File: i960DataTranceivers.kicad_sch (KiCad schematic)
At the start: 6 parts

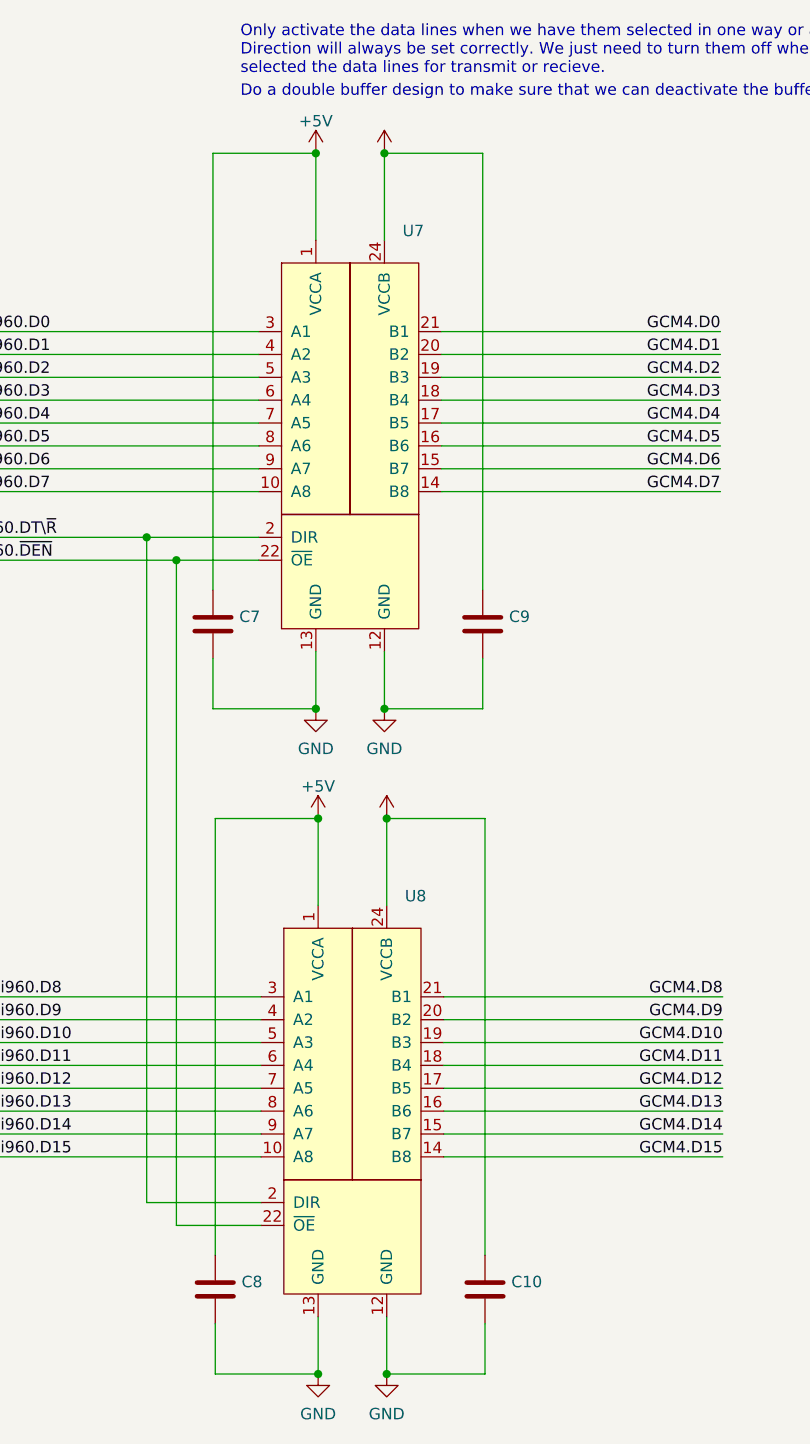
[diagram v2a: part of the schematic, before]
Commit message: Fix naming + more features
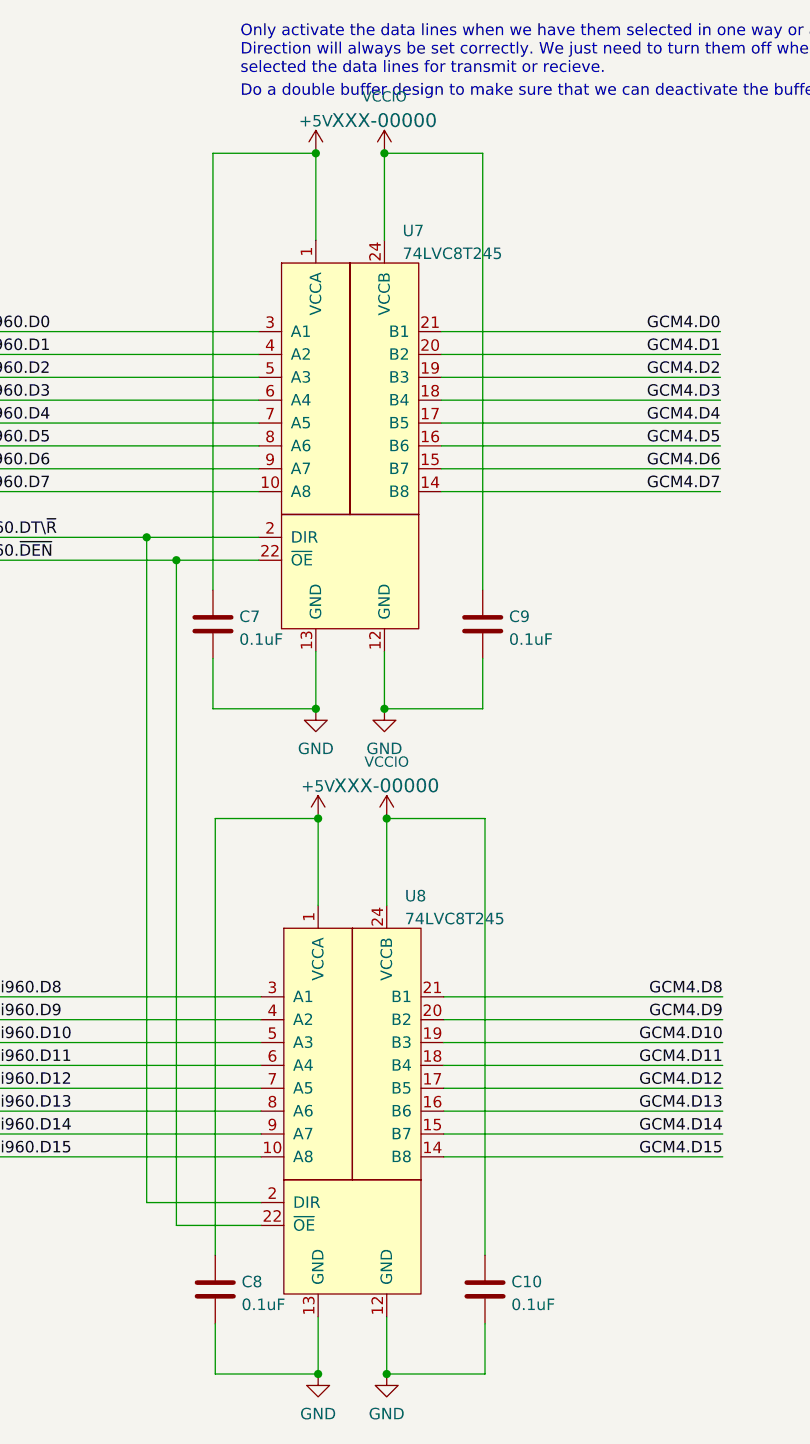
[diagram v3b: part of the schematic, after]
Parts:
- C10, C7, C8, C9: value (none) -> 0.1uF; footprint (none) -> Capacitor_SMD:C_0805_2012Metric_Pad1.18x1.45mm_HandSolder
- U7, U8: value (none) -> 74LVC8T245; footprint (none) -> Package_SO:SOIC-24W_7.5x15.4mm_P1.27mm
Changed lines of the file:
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@@
       (effects (font (size 1.27 1.27)) (justify left))
     )
-    (property "Value" "" (id 1) (at 132.5754 36.3021 0)
-      (effects (font (size 1.27 1.27)) (justify left))
-    )
-    (property "Footprint" "" (id 2) (at 126.746 66.548 0)
+    (property "Value" "74LVC8T245" (id 1) (at 132.5754 36.3021 0)
+      (effects (font (size 1.27 1.27)) (justify left))
+    )
+    (property "Footprint" "Package_SO:SOIC-24W_7.5x15.4mm_P1.27mm" (id 2) (at 126.746 66.548 0)
       (effects (font (size 1.27 1.27)) hide)
     )
@@
       (effects (font (size 1.27 1.27)) (justify left))
     )
-    (property "Value" "" (id 1) (at 144.653 153.0862 0)
-      (effects (font (size 1.27 1.27)) (justify left))
-    )
-    (property "Footprint" "" (id 2) (at 142.6972 155.194 0)
+    (property "Value" "0.1uF" (id 1) (at 144.653 153.0862 0)
+      (effects (font (size 1.27 1.27)) (justify left))
+    )
+    (property "Footprint" "Capacitor_SMD:C_0805_2012Metric_Pad1.18x1.45mm_HandSolder" (id 2) (at 142.6972 155.194 0)
       (effects (font (size 1.27 1.27)) hide)
     )
@@
       (effects (font (size 1.27 1.27)) (justify left))
     )
-    (property "Value" "" (id 1) (at 114.681 153.0862 0)
-      (effects (font (size 1.27 1.27)) (justify left))
-    )
-    (property "Footprint" "" (id 2) (at 112.7252 155.194 0)
+    (property "Value" "0.1uF" (id 1) (at 114.681 153.0862 0)
+      (effects (font (size 1.27 1.27)) (justify left))
+    )
+    (property "Footprint" "Capacitor_SMD:C_0805_2012Metric_Pad1.18x1.45mm_HandSolder" (id 2) (at 112.7252 155.194 0)
       (effects (font (size 1.27 1.27)) hide)
     )
@@
       (effects (font (size 1.27 1.27)) (justify left))
     )
-    (property "Value" "" (id 1) (at 144.399 79.1722 0)
-      (effects (font (size 1.27 1.27)) (justify left))
-    )
-    (property "Footprint" "" (id 2) (at 142.4432 81.28 0)
+    (property "Value" "0.1uF" (id 1) (at 144.399 79.1722 0)
+      (effects (font (size 1.27 1.27)) (justify left))
+    )
+    (property "Footprint" "Capacitor_SMD:C_0805_2012Metric_Pad1.18x1.45mm_HandSolder" (id 2) (at 142.4432 81.28 0)
       (effects (font (size 1.27 1.27)) hide)
     )
@@
       (effects (font (size 1.27 1.27)) (justify left))
     )
-    (property "Value" "" (id 1) (at 132.8294 110.2161 0)
-      (effects (font (size 1.27 1.27)) (justify left))
-    )
-    (property "Footprint" "" (id 2) (at 127 140.462 0)
+    (property "Value" "74LVC8T245" (id 1) (at 132.8294 110.2161 0)
+      (effects (font (size 1.27 1.27)) (justify left))
+    )
+    (property "Footprint" "Package_SO:SOIC-24W_7.5x15.4mm_P1.27mm" (id 2) (at 127 140.462 0)
       (effects (font (size 1.27 1.27)) hide)
     )
@@
       (effects (font (size 1.27 1.27)) (justify left))
     )
-    (property "Value" "" (id 1) (at 114.427 79.1722 0)
-      (effects (font (size 1.27 1.27)) (justify left))
-    )
-    (property "Footprint" "" (id 2) (at 112.4712 81.28 0)
+    (property "Value" "0.1uF" (id 1) (at 114.427 79.1722 0)
+      (effects (font (size 1.27 1.27)) (justify left))
+    )
+    (property "Footprint" "Capacitor_SMD:C_0805_2012Metric_Pad1.18x1.45mm_HandSolder" (id 2) (at 112.4712 81.28 0)
       (effects (font (size 1.27 1.27)) hide)
     )
@@
       (effects (font (size 1.143 1.143)) (justify left bottom) hide)
     )
-    (property "Value" "" (id 1) (at 130.556 18.8643 0)
+    (property "Value" "VCCIO" (id 1) (at 130.556 18.8643 0)
       (effects (font (size 1.143 1.143)))
     )
-    (property "Footprint" "" (id 2) (at 130.556 21.5153 0)
+    (property "Footprint" "XXX-00000" (id 2) (at 130.556 21.5153 0)
       (effects (font (size 1.524 1.524)))
     )
@@
       (effects (font (size 1.143 1.143)) (justify left bottom) hide)
     )
-    (property "Value" "" (id 1) (at 130.81 92.7783 0)
+    (property "Value" "VCCIO" (id 1) (at 130.81 92.7783 0)
       (effects (font (size 1.143 1.143)))
     )
-    (property "Footprint" "" (id 2) (at 130.81 95.4293 0)
+    (property "Footprint" "XXX-00000" (id 2) (at 130.81 95.4293 0)
       (effects (font (size 1.524 1.524)))
     )
